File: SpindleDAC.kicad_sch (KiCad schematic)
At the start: 10 parts, among them J14 Spindle Out, U15 LTV-817S, U16 ${SIM.PARAMS}, U17 TL431DBZ, U18 ${SIM.PARAMS}

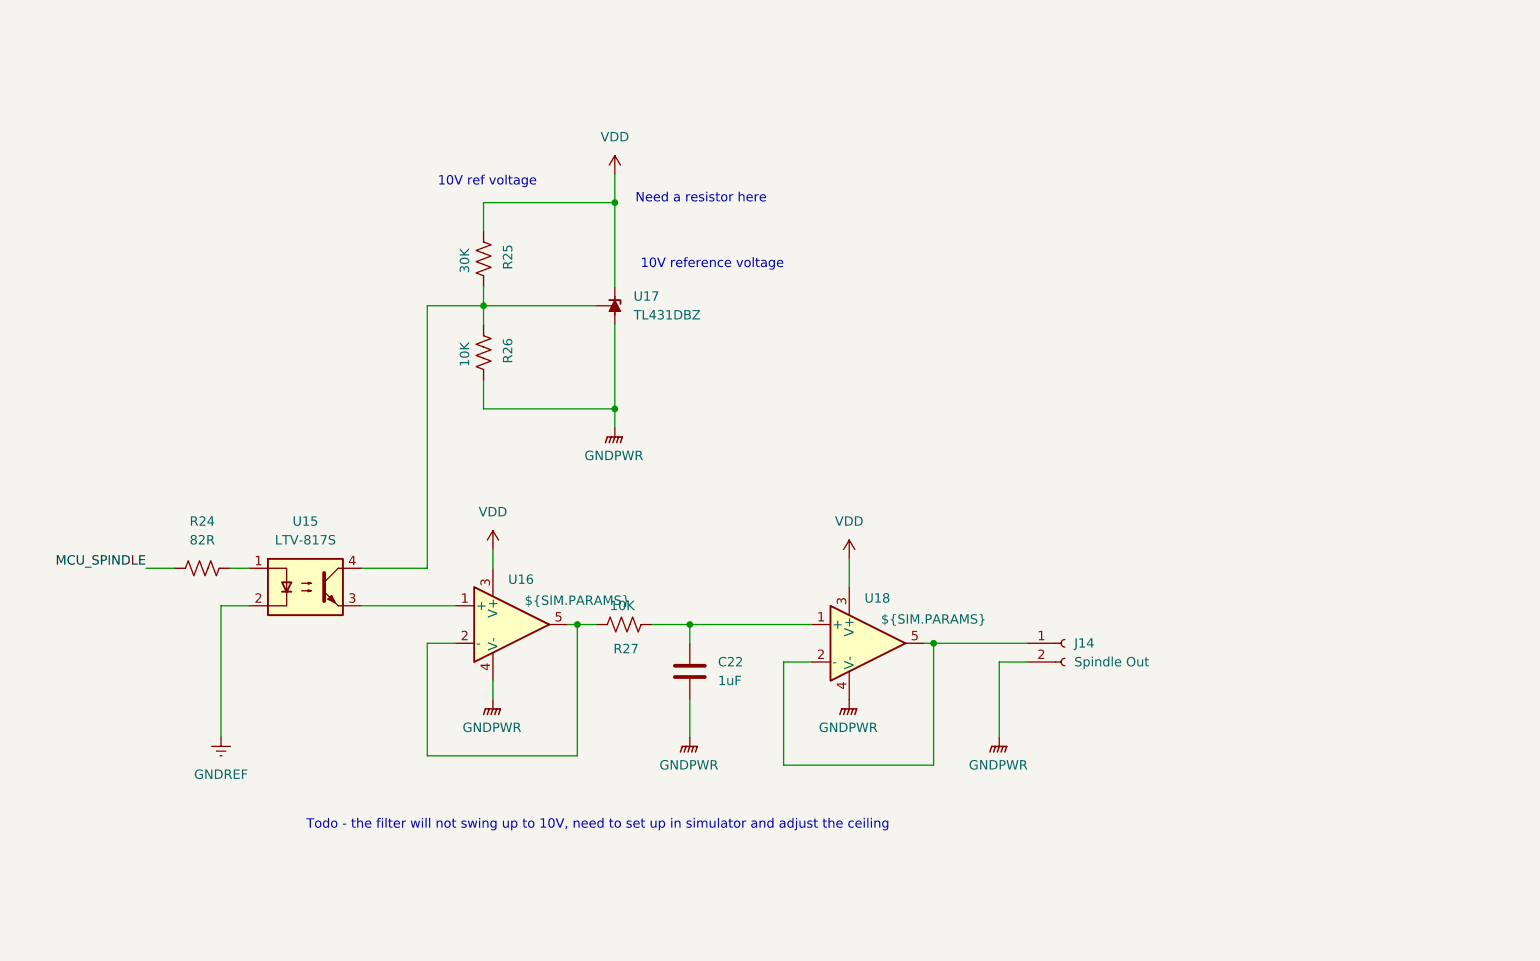
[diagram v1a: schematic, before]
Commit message: BOM consolidation for various resistors. Moved BOM into symbol libraries and updated supplimentary BOM. Switched IO optical isolation circuitry to a more cost effective part.
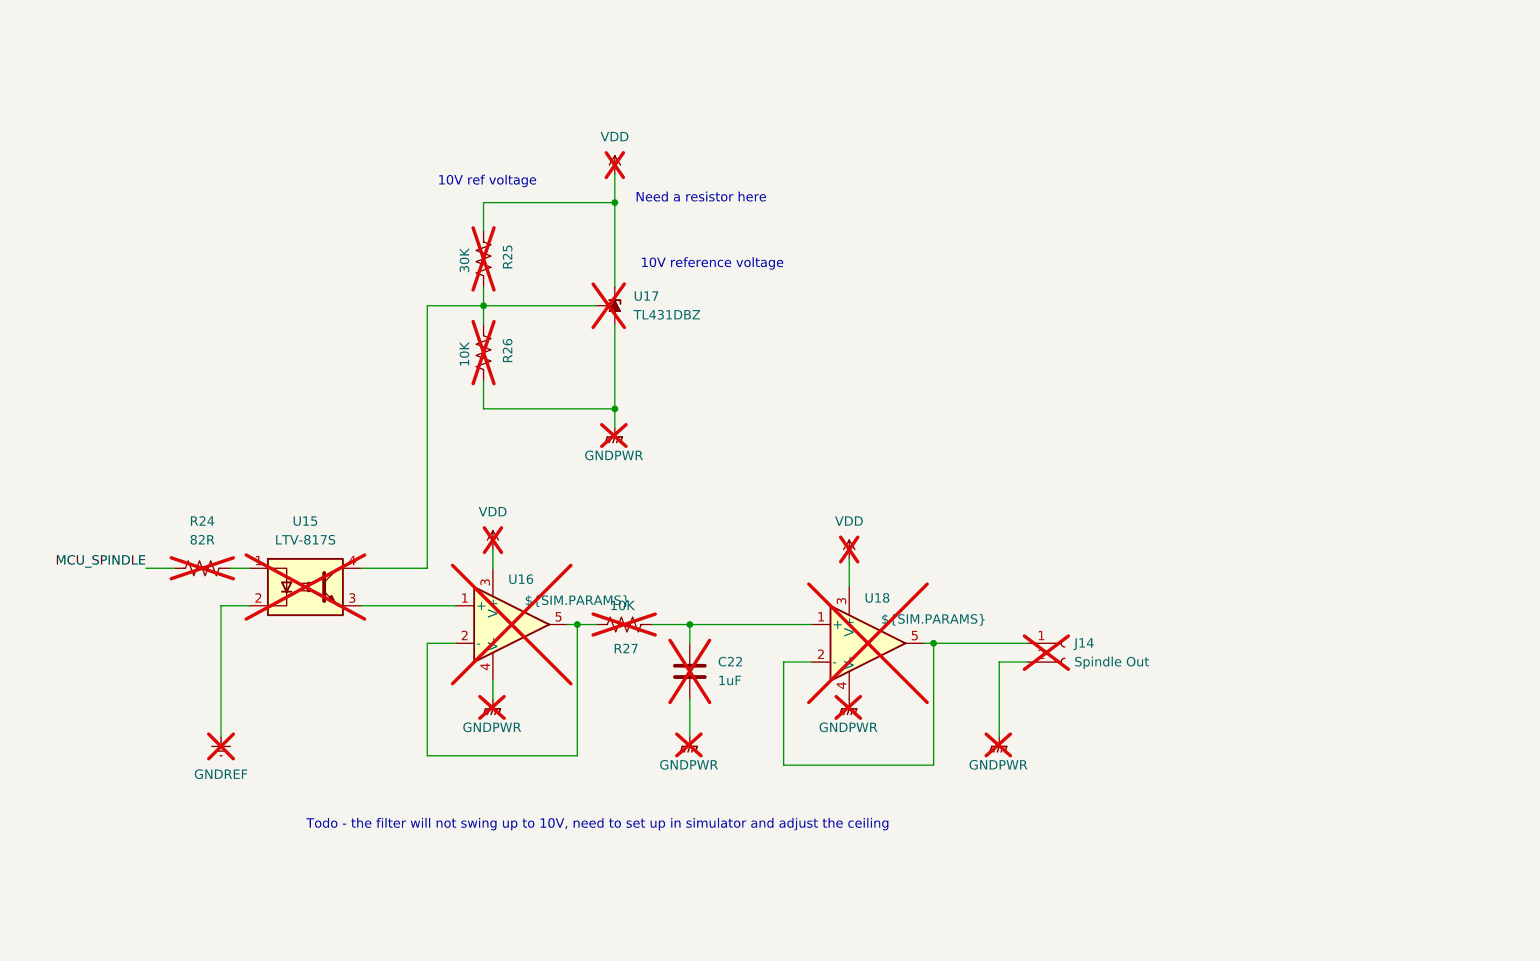
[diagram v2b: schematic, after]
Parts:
- C22, J14, R24, R25, U16, U17, U18: now not fitted
- R26, R27: Digikey Part Number (none) -> 311-10.0KFRCT-ND; Digikey URL (none) -> https://www.digikey.com.au/en/products/detail/yageo/RC1206F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; now not fitted
- U15: JLCPCB Part #（optional） C189217 -> (none); now not fitted
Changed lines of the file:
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@@
 		(exclude_from_sim no)
 		(in_bom yes)
-		(on_board yes)
-		(dnp no)
+		(on_board no)
+		(dnp yes)
 		(property "Reference" "U18"
 			(at 157.48 98.044 0)
@@
 		(exclude_from_sim no)
 		(in_bom yes)
-		(on_board yes)
-		(dnp no)
+		(on_board no)
+		(dnp yes)
 		(property "Reference" "R26"
 			(at 107.442 64.516 90)
@@
 			)
 		)
-		(property "Digikey Part Number" ""
+		(property "Digikey Part Number" "311-10.0KFRCT-ND "
 			(at 104.14 64.77 0)
 			(effects
@@
 			)
 		)
-		(property "Digikey URL" ""
+		(property "Digikey URL" "https://www.digikey.com.au/en/products/detail/yageo/RC1206FR-0710KL/728483 "
 			(at 104.14 64.77 0)
 			(effects
@@
 		(exclude_from_sim no)
 		(in_bom yes)
-		(on_board yes)
-		(dnp no)
+		(on_board no)
+		(dnp yes)
 		(fields_autoplaced yes)
 		(property "Reference" "R24"
@@
 		(exclude_from_sim no)
 		(in_bom yes)
-		(on_board yes)
-		(dnp no)
+		(on_board no)
+		(dnp yes)
 		(fields_autoplaced yes)
 		(property "Reference" "C22"
@@
 		(in_bom yes)
 		(on_board no)
-		(dnp no)
+		(dnp yes)
 		(fields_autoplaced yes)
 		(property "Reference" "#PWR0130"
@@
 		(exclude_from_sim no)
 		(in_bom yes)
-		(on_board yes)
-		(dnp no)
+		(on_board no)
+		(dnp yes)
 		(fields_autoplaced yes)
 		(property "Reference" "U15"
@@
 			)
 		)
-		(property "JLCPCB Part #（optional）" "C189217"
+		(property "JLCPCB Part #（optional）" ""
 			(at 80.01 96.52 0)
 			(effects
@@
 		(in_bom yes)
 		(on_board no)
-		(dnp no)
+		(dnp yes)
 		(fields_autoplaced yes)
 		(property "Reference" "#PWR0125"
@@
 		(exclude_from_sim no)
 		(in_bom yes)
-		(on_board yes)
-		(dnp no)
+		(on_board no)
+		(dnp yes)
 		(fields_autoplaced yes)
 		(property "Reference" "J14"
@@
 		(in_bom yes)
 		(on_board no)
-		(dnp no)
+		(dnp yes)
 		(fields_autoplaced yes)
 		(property "Reference" "#PWR0124"
@@
 		(in_bom yes)
 		(on_board no)
-		(dnp no)
+		(dnp yes)
 		(fields_autoplaced yes)
 		(property "Reference" "#PWR0127"
@@
 		(exclude_from_sim no)
 		(in_bom yes)
-		(on_board yes)
-		(dnp no)
+		(on_board no)
+		(dnp yes)
 		(fields_autoplaced yes)
 		(property "Reference" "U17"
@@
 		(in_bom yes)
 		(on_board no)
-		(dnp no)
+		(dnp yes)
 		(fields_autoplaced yes)
 		(property "Reference" "#PWR0132"
@@
 		(exclude_from_sim no)
 		(in_bom yes)
-		(on_board yes)
-		(dnp no)
+		(on_board no)
+		(dnp yes)
 		(property "Reference" "R25"
 			(at 107.442 51.816 90)
@@
 		(in_bom yes)
 		(on_board no)
-		(dnp no)
+		(dnp yes)
 		(fields_autoplaced yes)
 		(property "Reference" "#PWR0131"
@@
 		(exclude_from_sim no)
 		(in_bom yes)
-		(on_board yes)
-		(dnp no)
+		(on_board no)
+		(dnp yes)
 		(property "Reference" "R27"
 			(at 123.444 104.902 90)
@@
 			)
 		)
-		(property "Digikey Part Number" ""
+		(property "Digikey Part Number" "311-10.0KFRCT-ND "
 			(at 123.19 101.6 0)
 			(effects
@@
 			)
 		)
-		(property "Digikey URL" ""
+		(property "Digikey URL" "https://www.digikey.com.au/en/products/detail/yageo/RC1206FR-0710KL/728483 "
 			(at 123.19 101.6 0)
 			(effects
@@
 		(in_bom yes)
 		(on_board no)
-		(dnp no)
+		(dnp yes)
 		(fields_autoplaced yes)
 		(property "Reference" "#PWR0128"
@@
 		(in_bom yes)
 		(on_board no)
-		(dnp no)
+		(dnp yes)
 		(fields_autoplaced yes)
 		(property "Reference" "#PWR0129"
@@
 		(in_bom yes)
 		(on_board no)
-		(dnp no)
+		(dnp yes)
 		(fields_autoplaced yes)
 		(property "Reference" "#PWR0126"
@@
 		(exclude_from_sim no)
 		(in_bom yes)
-		(on_board yes)
-		(dnp no)
+		(on_board no)
+		(dnp yes)
 		(property "Reference" "U16"
 			(at 109.22 95.504 0)

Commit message: New PSU designs + footprints assigned. Changes to board shape to make room for new components. BOM consolidation of supplimentary file
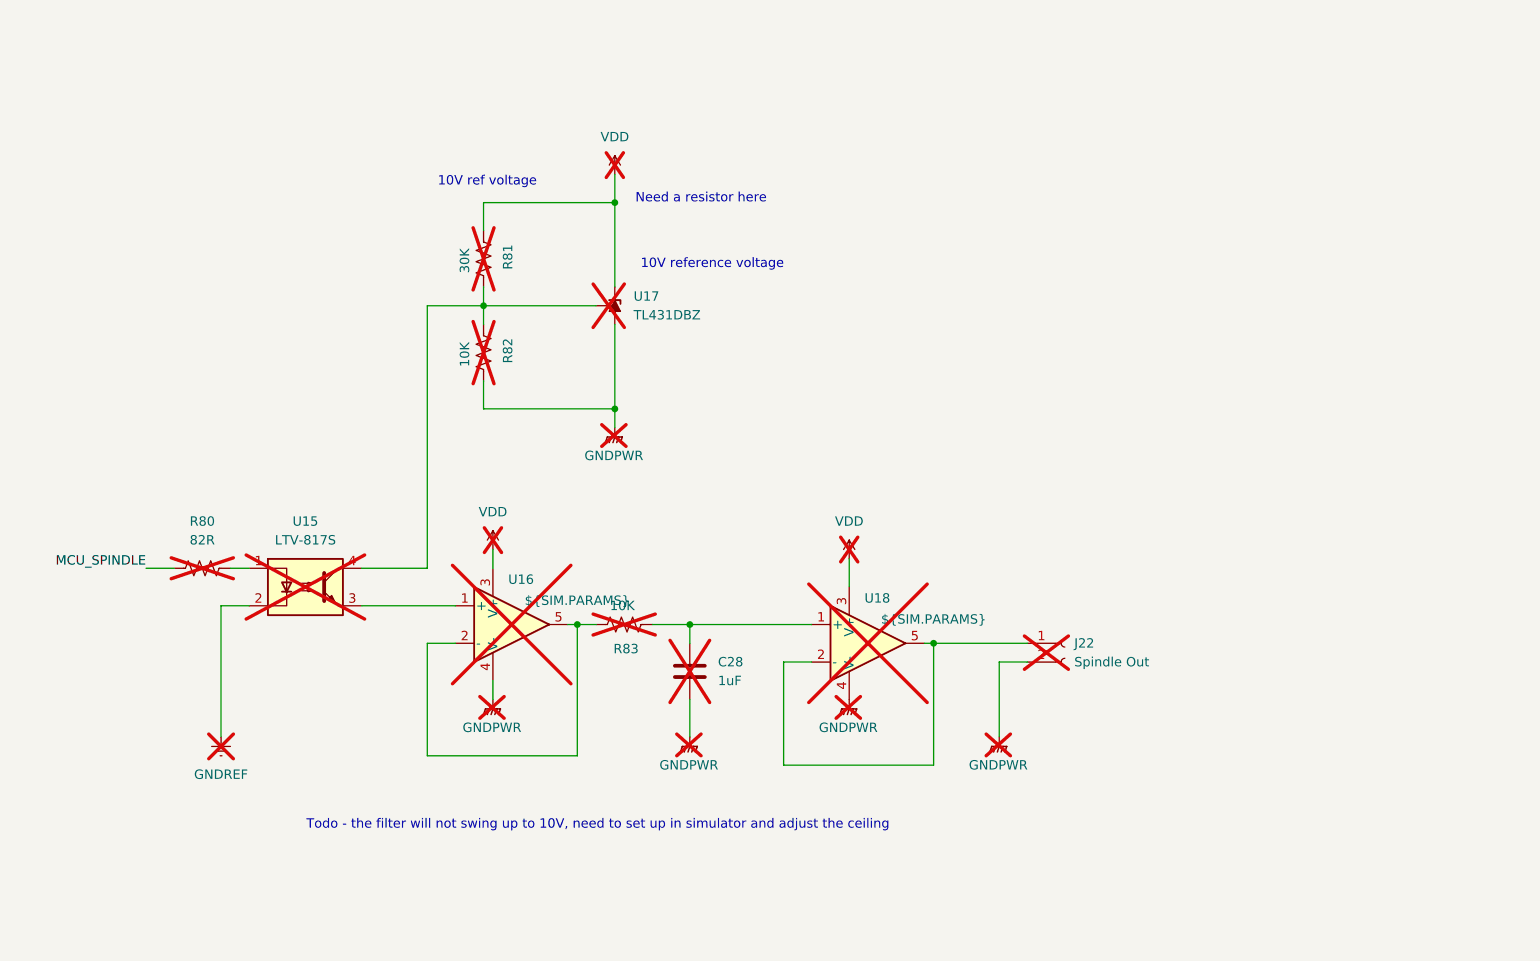
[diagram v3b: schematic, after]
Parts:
- renumbered C22 to C28, J14 to J22, R24 to R80, R25 to R81, R26 to R82, R27 to R83
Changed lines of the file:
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@@
 		(on_board no)
 		(dnp yes)
-		(property "Reference" "R26"
+		(property "Reference" "R82"
 			(at 107.442 64.516 90)
 			(effects
@@
 			(project "Remora Nucleo F446ZE Hat"
 				(path "/5473abc6-7b93-43cc-a401-f691c4d7d7cf/5cdad347-c6ad-4791-9d53-e4d1ad999196"
-					(reference "R26")
+					(reference "R82")
 					(unit 1)
 				)
@@
 		(dnp yes)
 		(fields_autoplaced yes)
-		(property "Reference" "R24"
+		(property "Reference" "R80"
 			(at 66.04 87.63 90)
 			(effects
@@
 			(project "Remora Nucleo F446ZE Hat"
 				(path "/5473abc6-7b93-43cc-a401-f691c4d7d7cf/5cdad347-c6ad-4791-9d53-e4d1ad999196"
-					(reference "R24")
+					(reference "R80")
 					(unit 1)
 				)
@@
 		(dnp yes)
 		(fields_autoplaced yes)
-		(property "Reference" "C22"
+		(property "Reference" "C28"
 			(at 135.89 106.6799 0)
 			(effects
@@
 			(project ""
 				(path "/5473abc6-7b93-43cc-a401-f691c4d7d7cf/5cdad347-c6ad-4791-9d53-e4d1ad999196"
-					(reference "C22")
+					(reference "C28")
 					(unit 1)
 				)
@@
 		(dnp yes)
 		(fields_autoplaced yes)
-		(property "Reference" "#PWR0130"
+		(property "Reference" "#PWR0199"
 			(at 153.67 96.52 0)
 			(effects
@@
 			(project "Remora Nucleo F446ZE Hat"
 				(path "/5473abc6-7b93-43cc-a401-f691c4d7d7cf/5cdad347-c6ad-4791-9d53-e4d1ad999196"
-					(reference "#PWR0130")
+					(reference "#PWR0199")
 					(unit 1)
 				)
@@
 		(dnp yes)
 		(fields_autoplaced yes)
-		(property "Reference" "#PWR0125"
+		(property "Reference" "#PWR0194"
 			(at 105.41 95.25 0)
 			(effects
@@
 			(project "Remora Nucleo F446ZE Hat"
 				(path "/5473abc6-7b93-43cc-a401-f691c4d7d7cf/5cdad347-c6ad-4791-9d53-e4d1ad999196"
-					(reference "#PWR0125")
+					(reference "#PWR0194")
 					(unit 1)
 				)
@@
 		(dnp yes)
 		(fields_autoplaced yes)
-		(property "Reference" "J14"
+		(property "Reference" "J22"
 			(at 184.15 104.1399 0)
 			(effects
@@
 			(project ""
 				(path "/5473abc6-7b93-43cc-a401-f691c4d7d7cf/5cdad347-c6ad-4791-9d53-e4d1ad999196"
-					(reference "J14")
+					(reference "J22")
 					(unit 1)
 				)
@@
 		(dnp yes)
 		(fields_autoplaced yes)
-		(property "Reference" "#PWR0124"
+		(property "Reference" "#PWR0193"
 			(at 68.58 123.19 0)
 			(effects
@@
 			(project "Remora Nucleo F446ZE Hat"
 				(path "/5473abc6-7b93-43cc-a401-f691c4d7d7cf/5cdad347-c6ad-4791-9d53-e4d1ad999196"
-					(reference "#PWR0124")
+					(reference "#PWR0193")
 					(unit 1)
 				)
@@
 		(dnp yes)
 		(fields_autoplaced yes)
-		(property "Reference" "#PWR0127"
+		(property "Reference" "#PWR0196"
 			(at 121.92 44.45 0)
 			(effects
@@
 			(project "Remora Nucleo F446ZE Hat"
 				(path "/5473abc6-7b93-43cc-a401-f691c4d7d7cf/5cdad347-c6ad-4791-9d53-e4d1ad999196"
-					(reference "#PWR0127")
+					(reference "#PWR0196")
 					(unit 1)
 				)
@@
 		(dnp yes)
 		(fields_autoplaced yes)
-		(property "Reference" "#PWR0132"
+		(property "Reference" "#PWR0201"
 			(at 173.99 121.92 0)
 			(effects
@@
 			(project "Remora Nucleo F446ZE Hat"
 				(path "/5473abc6-7b93-43cc-a401-f691c4d7d7cf/5cdad347-c6ad-4791-9d53-e4d1ad999196"
-					(reference "#PWR0132")
+					(reference "#PWR0201")
 					(unit 1)
 				)
@@
 		(on_board no)
 		(dnp yes)
-		(property "Reference" "R25"
+		(property "Reference" "R81"
 			(at 107.442 51.816 90)
 			(effects
@@
 			(project "Remora Nucleo F446ZE Hat"
 				(path "/5473abc6-7b93-43cc-a401-f691c4d7d7cf/5cdad347-c6ad-4791-9d53-e4d1ad999196"
-					(reference "R25")
+					(reference "R81")
 					(unit 1)
 				)
@@
 		(dnp yes)
 		(fields_autoplaced yes)
-		(property "Reference" "#PWR0131"
+		(property "Reference" "#PWR0200"
 			(at 153.67 116.84 0)
 			(effects
@@
 			(project "Remora Nucleo F446ZE Hat"
 				(path "/5473abc6-7b93-43cc-a401-f691c4d7d7cf/5cdad347-c6ad-4791-9d53-e4d1ad999196"
-					(reference "#PWR0131")
+					(reference "#PWR0200")
 					(unit 1)
 				)
@@
 		(on_board no)
 		(dnp yes)
-		(property "Reference" "R27"
+		(property "Reference" "R83"
 			(at 123.444 104.902 90)
 			(effects
@@
 			(project "Remora Nucleo F446ZE Hat"
 				(path "/5473abc6-7b93-43cc-a401-f691c4d7d7cf/5cdad347-c6ad-4791-9d53-e4d1ad999196"
-					(reference "R27")
+					(reference "R83")
 					(unit 1)
 				)
@@
 		(dnp yes)
 		(fields_autoplaced yes)
-		(property "Reference" "#PWR0128"
+		(property "Reference" "#PWR0197"
 			(at 121.92 80.01 0)
 			(effects
@@
 			(project "Remora Nucleo F446ZE Hat"
 				(path "/5473abc6-7b93-43cc-a401-f691c4d7d7cf/5cdad347-c6ad-4791-9d53-e4d1ad999196"
-					(reference "#PWR0128")
+					(reference "#PWR0197")
 					(unit 1)
 				)
@@
 		(dnp yes)
 		(fields_autoplaced yes)
-		(property "Reference" "#PWR0129"
+		(property "Reference" "#PWR0198"
 			(at 132.08 121.92 0)
 			(effects
@@
 			(project "Remora Nucleo F446ZE Hat"
 				(path "/5473abc6-7b93-43cc-a401-f691c4d7d7cf/5cdad347-c6ad-4791-9d53-e4d1ad999196"
-					(reference "#PWR0129")
+					(reference "#PWR0198")
 					(unit 1)
 				)
@@
 		(dnp yes)
 		(fields_autoplaced yes)
-		(property "Reference" "#PWR0126"
+		(property "Reference" "#PWR0195"
 			(at 105.41 116.84 0)
 			(effects
@@
 			(project "Remora Nucleo F446ZE Hat"
 				(path "/5473abc6-7b93-43cc-a401-f691c4d7d7cf/5cdad347-c6ad-4791-9d53-e4d1ad999196"
-					(reference "#PWR0126")
-					(unit 1)
-				)
+					(reference "#PWR0195")
+					(unit 1)
+				)

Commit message: Added Analog inputs, updates to readme re powering board from external supply
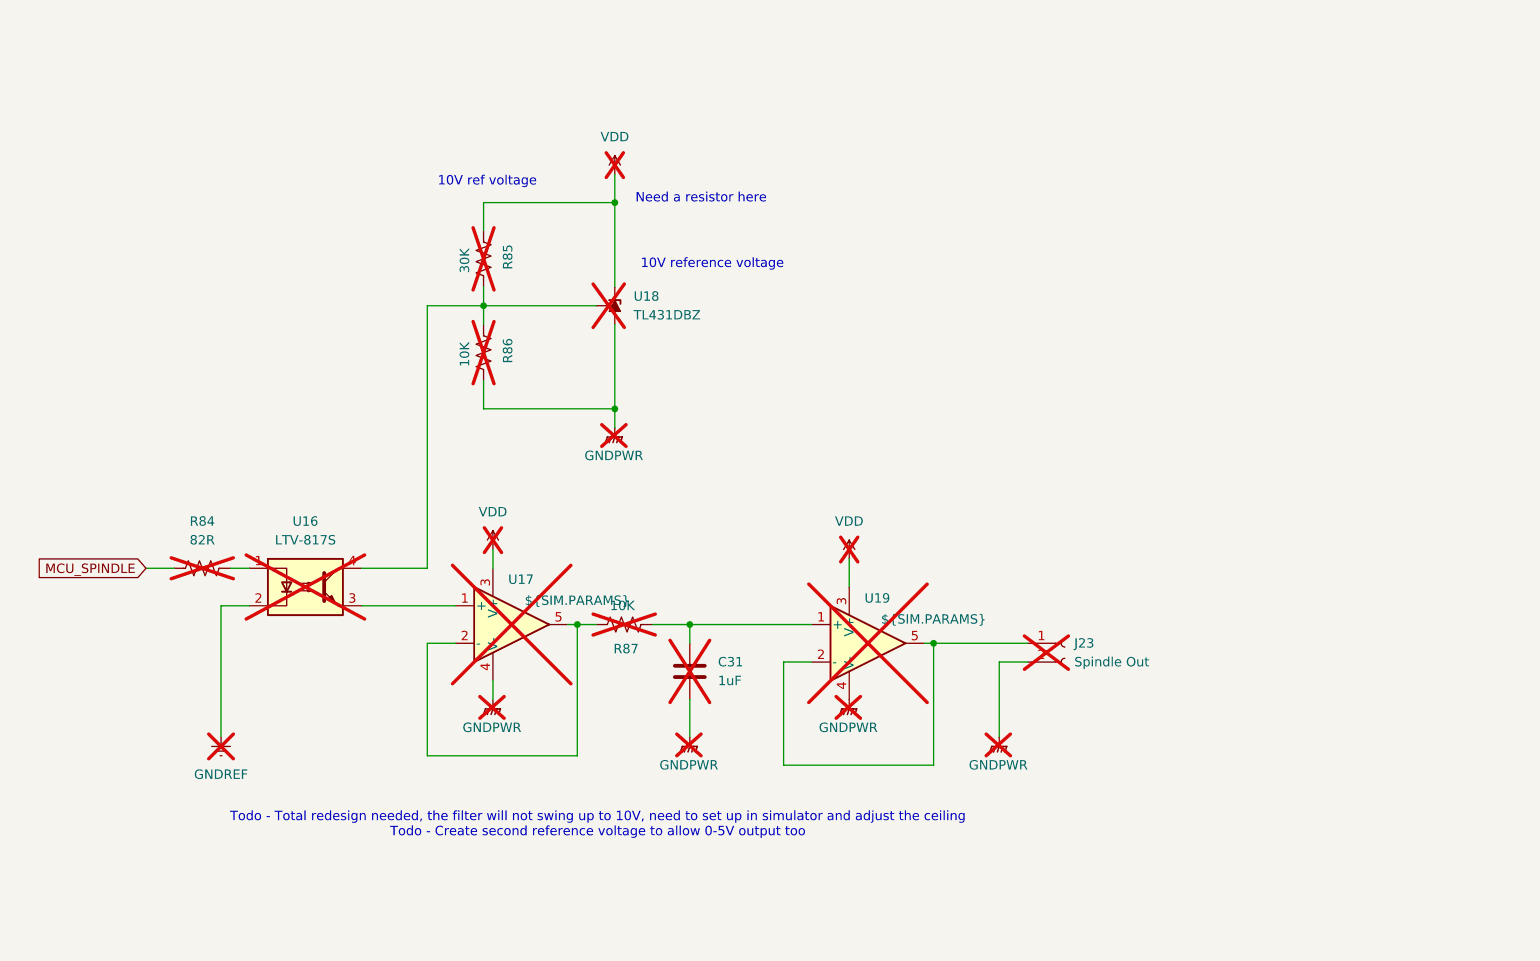
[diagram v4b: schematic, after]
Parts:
- renumbered C28 to C31, J22 to J23, R80 to R84, R81 to R85, R82 to R86, R83 to R87, U15 to U16, U16 to U17, U17 to U18, U18 to U19
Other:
- note added: "Todo - Total redesign needed, the filter will not swing up to 10V, need to set up in simulator and adjust the ceiling Todo - Create second reference voltage to allow 0-5V output too"
- note removed: "Todo - the filter will not swing up to 10V, need to set up in simulator and adjust the ceiling"
